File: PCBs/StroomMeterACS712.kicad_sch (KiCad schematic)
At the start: 8 parts, among them J1 OLED1604, J2 ACS712, J3 PWR_5V, J4 WS2812, Q1 BC547, Q2 BC547, U1 WeMos_D1_mini

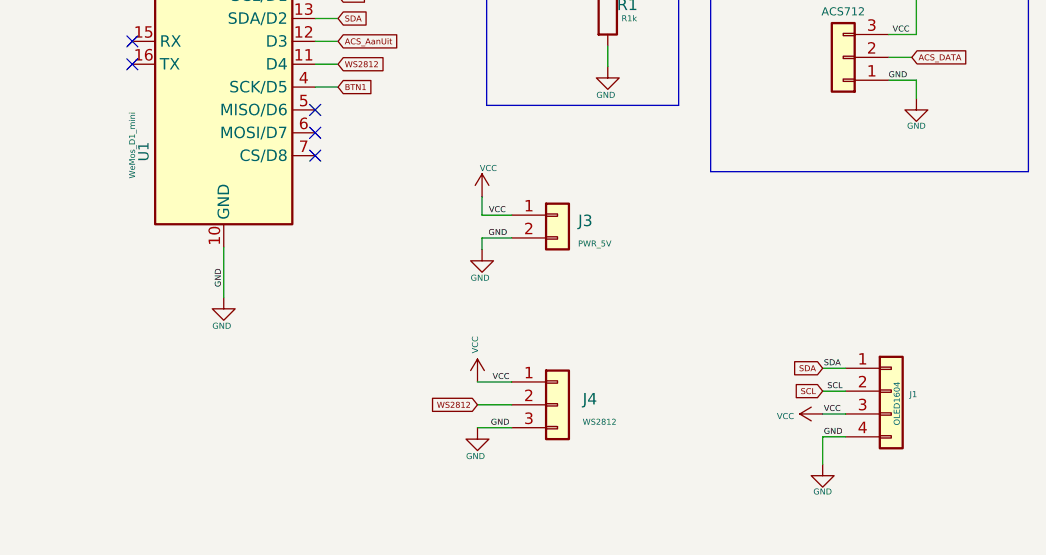
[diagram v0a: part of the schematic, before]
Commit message: WS2812 toegevoegd
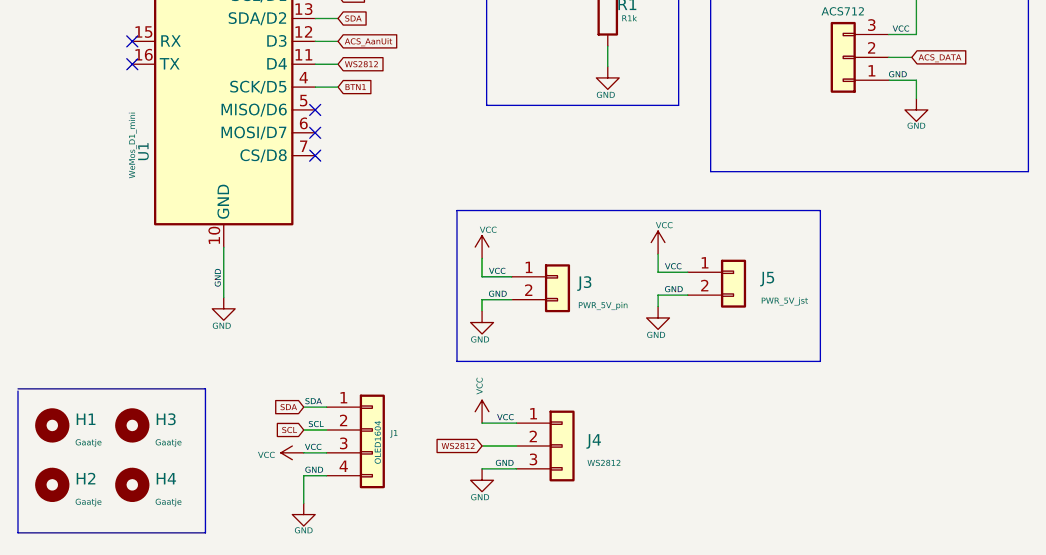
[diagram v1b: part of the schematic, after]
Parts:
- added H1, H2, H3, H4: Gaatje, MountingHole:MountingHole_3.2mm_M3, symbol Mechanical:MountingHole
- added J5: PWR_5V_jst, Connector_JST:JST_EH_B2B-EH-A_1x02_P2.50mm_Vertical, symbol Connector_Generic:Conn_01x02
- J1: footprint (none) -> Display:Adafruit_SSD1306
- J2: footprint (none) -> Connector_PinHeader_2.00mm:PinHeader_1x03_P2.00mm_Vertical
- J3: value PWR_5V -> PWR_5V_pin; footprint (none) -> Connector_PinHeader_2.00mm:PinHeader_1x02_P2.00mm_Vertical_SMD_Pin1Right
- J4: footprint (none) -> Connector_PinHeader_2.00mm:PinHeader_1x04_P2.00mm_Horizontal
- R1: footprint (none) -> Resistor_THT:R_Axial_DIN0204_L3.6mm_D1.6mm_P7.62mm_Horizontal
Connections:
- net GND: now also J5.2 (Pin_2)
- net VCC: now also J5.1 (Pin_1)
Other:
- moved on the sheet: J1, J3, J4

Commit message: PCb toegeovegd
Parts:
- added SW1: btnAanUit, Button_Switch_THT:KSA_Tactile_SPST, symbol Switch:SW_Push
- H1, H2, H3, H4: footprint MountingHole:MountingHole_3.2mm_M3 -> MountingHole:MountingHole_2.7mm_M2.5_Pad
- J1: footprint Display:Adafruit_SSD1306 -> Connector_PinHeader_2.00mm:PinHeader_1x03_P2.00mm_Vertical
- R1: value R1k -> R100
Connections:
- net BTN1: now also SW1.1; no longer Q2.2 (B)
- net GND: now also Q2.3 (E); no longer R1.2
- net at R1.1: now also SW1.2; no longer Q2.3 (E)
- new net: Q2.2 (B), R1.2
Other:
- moved on the sheet: Q2, R1

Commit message: bijgewerkt
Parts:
- added K1: SRD-03VDC-SL-C, Relay_THT:Relay_SPDT_SANYOU_SRD_Series_Form_C, symbol Relay:SANYOU_SRD_Form_C
- added R2, R3, R4: R10K, symbol Device:R_Small_US
- added SW2: SW_SPDT, symbol Switch:SW_SPDT
- added U2: PCF8574A, symbol Interface_Expansion:PCF8574A
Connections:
- net GND: now also U2.8 (VSS)
- net SDA: now also U2.14 (SCL), U2.15 (SDA)
- new net: R2.2, U2.2 (A1)
- new net: R3.2, U2.1 (A0)
- new net: R4.2, U2.3 (A2)
- new net +5V: R2.1, R3.1, R4.1
- no-connect marks 6 -> 7

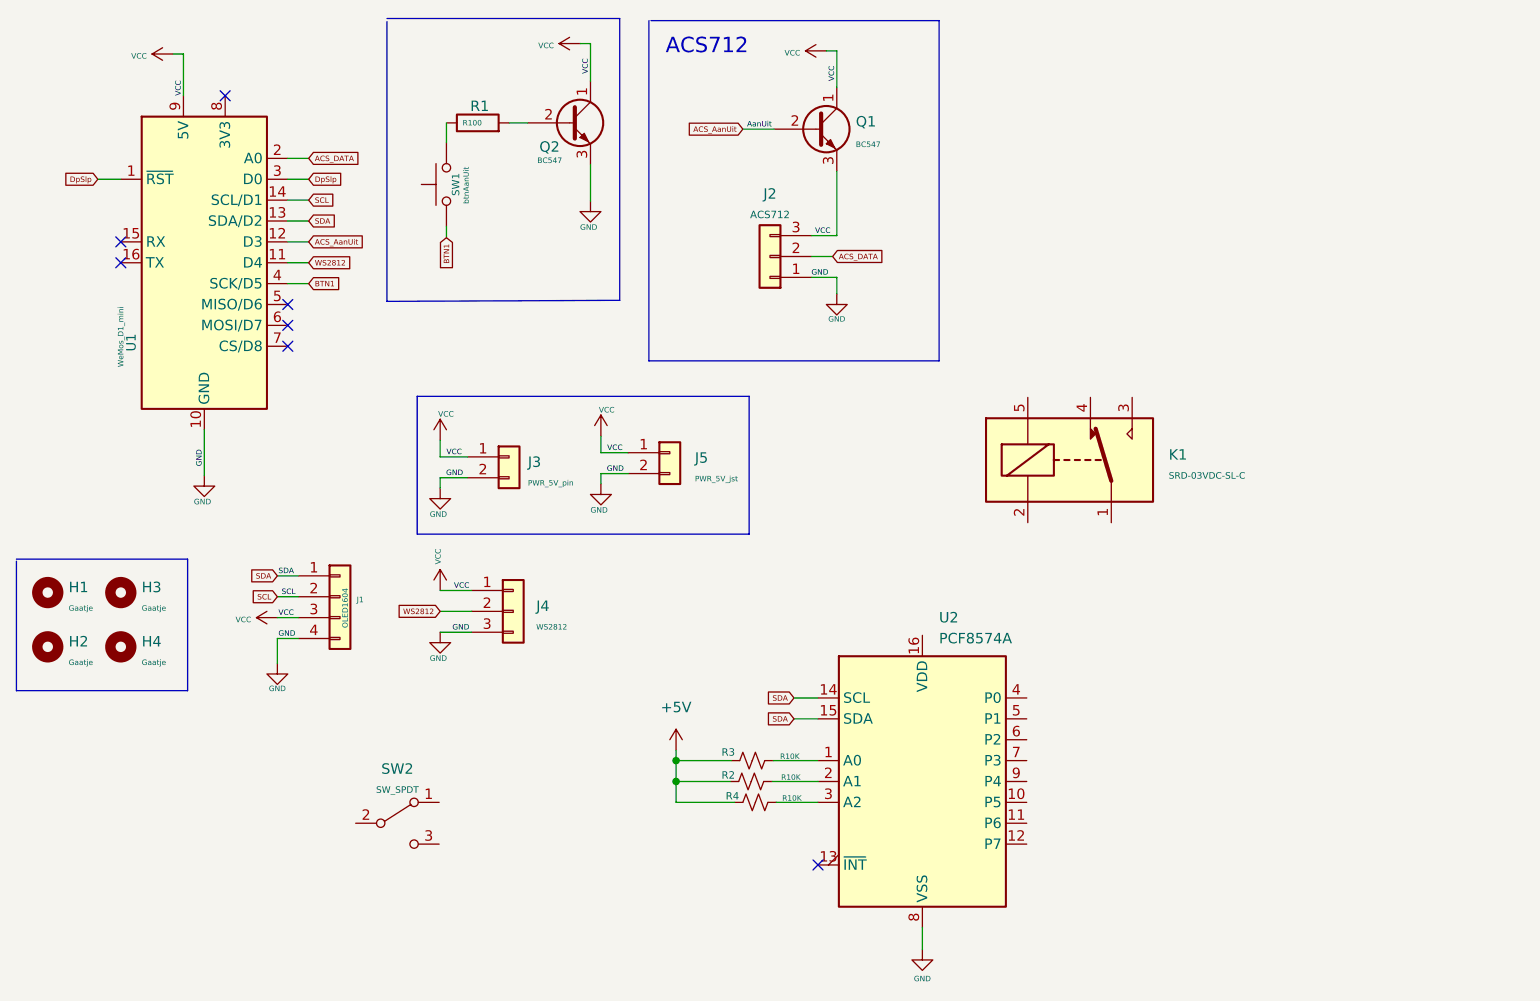
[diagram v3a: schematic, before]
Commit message: PCF8574 toegevoegd
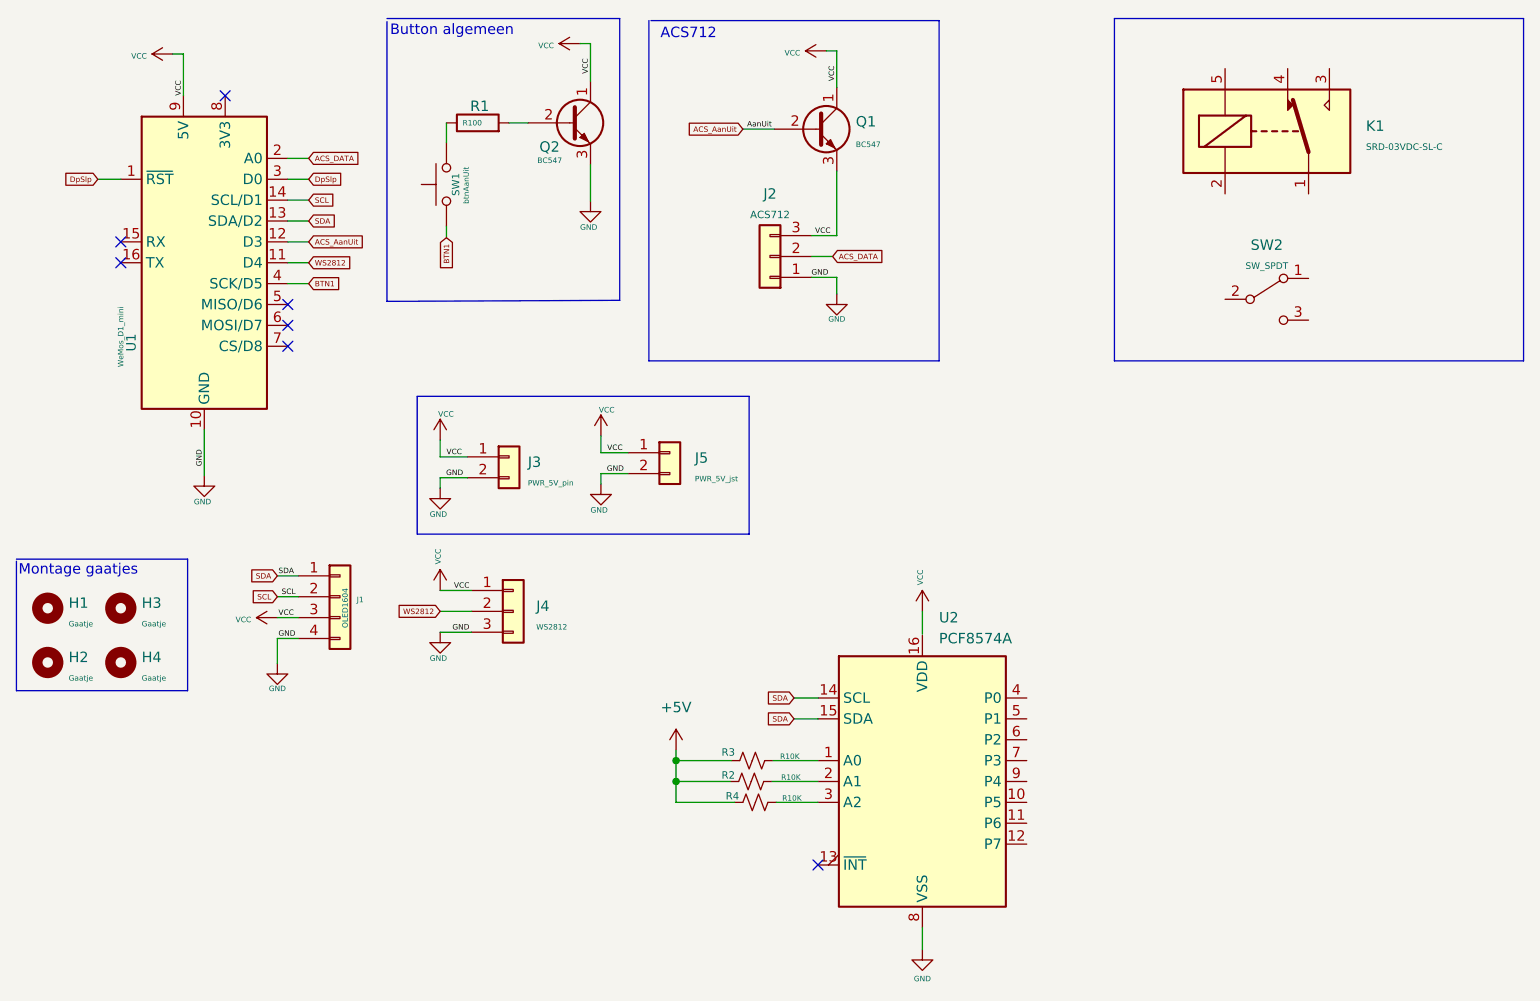
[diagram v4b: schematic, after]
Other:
- note added: "Button algemeen"
- note added: "Montage gaatjes"
- moved on the sheet: H1, H2, H3, H4, K1, SW2
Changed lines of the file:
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@@
+    (stroke (width 0) (type default) (color 0 0 0 0))
+  )
+  (polyline (pts (xy 156.464 19.812) (xy 206.248 19.812))
     (stroke (width 0) (type default) (color 0 0 0 0))
   )
@@
     (stroke (width 0) (type default) (color 0 0 0 0))
   )
+  (polyline (pts (xy 206.248 61.468) (xy 156.464 61.468))
+    (stroke (width 0) (type default) (color 0 0 0 0))
+  )
   (wire (pts (xy 117.475 105.029) (xy 120.396 105.029))
     (stroke (width 0) (type default) (color 0 0 0 0))
@@
     (stroke (width 0) (type default) (color 0 0 0 0))
   )
+  (polyline (pts (xy 156.464 19.812) (xy 156.464 61.468))
+    (stroke (width 0) (type default) (color 0 0 0 0))
+  )
   (wire (pts (xy 93.98 70.612) (xy 93.98 72.644))
     (stroke (width 0) (type default) (color 0 0 0 0))
@@
     (stroke (width 0) (type default) (color 0 0 0 0))
   )
+  (wire (pts (xy 133.096 91.948) (xy 133.096 94.742))
+    (stroke (width 0) (type default) (color 0 0 0 0))
+  )
   (wire (pts (xy 54.61 95.25) (xy 57.15 95.25))
     (stroke (width 0) (type default) (color 0 0 0 0))
@@
     (stroke (width 0) (type default) (color 0 0 0 0))
   )
+  (polyline (pts (xy 206.248 19.812) (xy 206.248 61.468))
+    (stroke (width 0) (type default) (color 0 0 0 0))
+  )
   (wire (pts (xy 75.184 46.482) (xy 75.184 45.085))
     (stroke (width 0) (type default) (color 0 0 0 0))
@@
     (stroke (width 0) (type default) (color 0 0 0 0))
   )
-  (text "ACS712" (at 101.854 24.384 0)
-    (effects (font (size 1.87 1.87)) (justify left bottom))
+  (text "Montage gaatjes" (at 23.114 87.757 0)
+    (effects (font (size 1.27 1.27)) (justify left bottom))
+  )
+  (text "Button algemeen" (at 68.326 22.098 0)
+    (effects (font (size 1.27 1.27)) (justify left bottom))
+  )
+  (text "ACS712" (at 101.219 22.479 0)
+    (effects (font (size 1.27 1.27)) (justify left bottom))
   )
   (label "VCC" (at 54.737 92.71 0)
@@
     (pin "2")
   )
-  (symbol (lib_id "Relay:SANYOU_SRD_Form_C") (at 151.003 73.533 0) (unit 1)
-    (in_bom yes) (on_board yes) (fields_autoplaced)
-    (property "Reference" "K1" (id 0) (at 163.068 72.8979 0)
-      (effects (font (size 1.27 1.27)) (justify left))
-    )
-    (property "Value" "SRD-03VDC-SL-C" (id 1) (at 163.068 75.438 0)
+  (symbol (lib_id "Relay:SANYOU_SRD_Form_C") (at 175.006 33.528 0) (unit 1)
+    (in_bom yes) (on_board yes) (fields_autoplaced)
+    (property "Reference" "K1" (id 0) (at 187.071 32.8929 0)
+      (effects (font (size 1.27 1.27)) (justify left))
+    )
+    (property "Value" "SRD-03VDC-SL-C" (id 1) (at 187.071 35.433 0)
       (effects (font (size 0.8 0.8)) (justify left))
     )
-    (property "Footprint" "Relay_THT:Relay_SPDT_SANYOU_SRD_Series_Form_C" (id 2) (at 162.433 74.803 0)
+    (property "Footprint" "Relay_THT:Relay_SPDT_SANYOU_SRD_Series_Form_C" (id 2) (at 186.436 34.798 0)
       (effects (font (size 1.27 1.27)) (justify left) hide)
     )
-    (property "Datasheet" "http://www.sanyourelay.ca/public/products/pdf/SRD.pdf" (id 3) (at 151.003 73.533 0)
+    (property "Datasheet" "http://www.sanyourelay.ca/public/products/pdf/SRD.pdf" (id 3) (at 175.006 33.528 0)
       (effects (font (size 1.27 1.27)) hide)
     )
@@
     (pin "2")
   )
-  (symbol (lib_id "Mechanical:MountingHole") (at 26.67 96.266 0) (unit 1)
-    (in_bom yes) (on_board yes) (fields_autoplaced)
-    (property "Reference" "H2" (id 0) (at 29.21 95.6309 0)
-      (effects (font (size 1.27 1.27)) (justify left))
-    )
-    (property "Value" "Gaatje" (id 1) (at 29.21 98.171 0)
+  (symbol (lib_id "Mechanical:MountingHole") (at 26.67 98.171 0) (unit 1)
+    (in_bom yes) (on_board yes) (fields_autoplaced)
+    (property "Reference" "H2" (id 0) (at 29.21 97.5359 0)
+      (effects (font (size 1.27 1.27)) (justify left))
+    )
+    (property "Value" "Gaatje" (id 1) (at 29.21 100.076 0)
       (effects (font (size 0.66 0.66)) (justify left))
     )
-    (property "Footprint" "MountingHole:MountingHole_2.7mm_M2.5_Pad" (id 2) (at 26.67 96.266 0)
-      (effects (font (size 1.27 1.27)) hide)
-    )
-    (property "Datasheet" "~" (id 3) (at 26.67 96.266 0)
+    (property "Footprint" "MountingHole:MountingHole_2.7mm_M2.5_Pad" (id 2) (at 26.67 98.171 0)
+      (effects (font (size 1.27 1.27)) hide)
+    )
+    (property "Datasheet" "~" (id 3) (at 26.67 98.171 0)
       (effects (font (size 1.27 1.27)) hide)
     )
@@
     (pin "2")
   )
-  (symbol (lib_id "Mechanical:MountingHole") (at 35.56 89.662 0) (unit 1)
-    (in_bom yes) (on_board yes) (fields_autoplaced)
-    (property "Reference" "H3" (id 0) (at 38.1 89.0269 0)
-      (effects (font (size 1.27 1.27)) (justify left))
-    )
-    (property "Value" "Gaatje" (id 1) (at 38.1 91.567 0)
+  (symbol (lib_id "Mechanical:MountingHole") (at 35.56 91.567 0) (unit 1)
+    (in_bom yes) (on_board yes) (fields_autoplaced)
+    (property "Reference" "H3" (id 0) (at 38.1 90.9319 0)
+      (effects (font (size 1.27 1.27)) (justify left))
+    )
+    (property "Value" "Gaatje" (id 1) (at 38.1 93.472 0)
       (effects (font (size 0.66 0.66)) (justify left))
     )
-    (property "Footprint" "MountingHole:MountingHole_2.7mm_M2.5_Pad" (id 2) (at 35.56 89.662 0)
-      (effects (font (size 1.27 1.27)) hide)
-    )
-    (property "Datasheet" "~" (id 3) (at 35.56 89.662 0)
+    (property "Footprint" "MountingHole:MountingHole_2.7mm_M2.5_Pad" (id 2) (at 35.56 91.567 0)
+      (effects (font (size 1.27 1.27)) hide)
+    )
+    (property "Datasheet" "~" (id 3) (at 35.56 91.567 0)
       (effects (font (size 1.27 1.27)) hide)
     )
@@
     (pin "1")
   )
-  (symbol (lib_id "Switch:SW_SPDT") (at 69.215 117.729 0) (unit 1)
-    (in_bom yes) (on_board yes) (fields_autoplaced)
-    (property "Reference" "SW2" (id 0) (at 69.215 111.125 0))
-    (property "Value" "SW_SPDT" (id 1) (at 69.215 113.665 0)
+  (symbol (lib_id "Switch:SW_SPDT") (at 175.006 53.975 0) (unit 1)
+    (in_bom yes) (on_board yes) (fields_autoplaced)
+    (property "Reference" "SW2" (id 0) (at 175.006 47.371 0))
+    (property "Value" "SW_SPDT" (id 1) (at 175.006 49.911 0)
       (effects (font (size 0.8 0.8)))
     )
-    (property "Footprint" "" (id 2) (at 69.215 117.729 0)
-      (effects (font (size 1.27 1.27)) hide)
-    )
-    (property "Datasheet" "~" (id 3) (at 69.215 117.729 0)
+    (property "Footprint" "" (id 2) (at 175.006 53.975 0)
+      (effects (font (size 1.27 1.27)) hide)
+    )
+    (property "Datasheet" "~" (id 3) (at 175.006 53.975 0)
       (effects (font (size 1.27 1.27)) hide)
     )
@@
     (pin "2")
   )
-  (symbol (lib_id "Mechanical:MountingHole") (at 35.56 96.266 0) (unit 1)
-    (in_bom yes) (on_board yes) (fields_autoplaced)
-    (property "Reference" "H4" (id 0) (at 38.1 95.6309 0)
-      (effects (font (size 1.27 1.27)) (justify left))
-    )
-    (property "Value" "Gaatje" (id 1) (at 38.1 98.171 0)
+  (symbol (lib_id "Mechanical:MountingHole") (at 35.56 98.171 0) (unit 1)
+    (in_bom yes) (on_board yes) (fields_autoplaced)
+    (property "Reference" "H4" (id 0) (at 38.1 97.5359 0)
+      (effects (font (size 1.27 1.27)) (justify left))
+    )
+    (property "Value" "Gaatje" (id 1) (at 38.1 100.076 0)
       (effects (font (size 0.66 0.66)) (justify left))
     )
-    (property "Footprint" "MountingHole:MountingHole_2.7mm_M2.5_Pad" (id 2) (at 35.56 96.266 0)
-      (effects (font (size 1.27 1.27)) hide)
-    )
-    (property "Datasheet" "~" (id 3) (at 35.56 96.266 0)
+    (property "Footprint" "MountingHole:MountingHole_2.7mm_M2.5_Pad" (id 2) (at 35.56 98.171 0)
+      (effects (font (size 1.27 1.27)) hide)
+    )
+    (property "Datasheet" "~" (id 3) (at 35.56 98.171 0)
       (effects (font (size 1.27 1.27)) hide)
     )
@@
     )
     (property "Datasheet" "" (id 3) (at 74.422 89.408 0)
+      (effects (font (size 1.27 1.27)) hide)
+    )
+    (pin "1")
+  )
+  (symbol (lib_id "power:VCC") (at 133.096 91.948 0) (unit 1)
+    (in_bom yes) (on_board yes)
+    (property "Reference" "#PWR08" (id 0) (at 133.096 95.758 0)
+      (effects (font (size 1.27 1.27)) hide)
+    )
+    (property "Value" "VCC" (id 1) (at 132.8433 88.7731 90)
+      (effects (font (size 0.67 0.67)) (justify left))
+    )
+    (property "Footprint" "" (id 2) (at 133.096 91.948 0)
+      (effects (font (size 1.27 1.27)) hide)
+    )
+    (property "Datasheet" "" (id 3) (at 133.096 91.948 0)
       (effects (font (size 1.27 1.27)) hide)
     )
@@
     (pin "1")
   )
-  (symbol (lib_id "Mechanical:MountingHole") (at 26.67 89.662 0) (unit 1)
-    (in_bom yes) (on_board yes) (fields_autoplaced)
-    (property "Reference" "H1" (id 0) (at 29.21 89.0269 0)
-      (effects (font (size 1.27 1.27)) (justify left))
-    )
-    (property "Value" "Gaatje" (id 1) (at 29.21 91.567 0)
+  (symbol (lib_id "Mechanical:MountingHole") (at 26.67 91.567 0) (unit 1)
+    (in_bom yes) (on_board yes) (fields_autoplaced)
+    (property "Reference" "H1" (id 0) (at 29.21 90.9319 0)
+      (effects (font (size 1.27 1.27)) (justify left))
+    )
+    (property "Value" "Gaatje" (id 1) (at 29.21 93.472 0)
       (effects (font (size 0.66 0.66)) (justify left))
     )
-    (property "Footprint" "MountingHole:MountingHole_2.7mm_M2.5_Pad" (id 2) (at 26.67 89.662 0)
-      (effects (font (size 1.27 1.27)) hide)
-    )
-    (property "Datasheet" "~" (id 3) (at 26.67 89.662 0)
+    (property "Footprint" "MountingHole:MountingHole_2.7mm_M2.5_Pad" (id 2) (at 26.67 91.567 0)
+      (effects (font (size 1.27 1.27)) hide)
+    )
+    (property "Datasheet" "~" (id 3) (at 26.67 91.567 0)
       (effects (font (size 1.27 1.27)) hide)
     )
@@
       (reference "#PWR07") (unit 1) (value "GND") (footprint "")
     )
+    (path "/e2adab14-7bfe-4689-8993-783208432c43"
+      (reference "#PWR08") (unit 1) (value "VCC") (footprint "")
+    )
     (path "/5baaad51-90c9-47e6-8528-1e99fbd4fc0a"

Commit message: Bijgewerkt
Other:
- note added: "220V Power regelaar"
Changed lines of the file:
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@@
+    (effects (font (size 1.27 1.27)) (justify left bottom))
+  )
+  (text "220V Power regelaar" (at 157.353 22.606 0)
     (effects (font (size 1.27 1.27)) (justify left bottom))
   )
